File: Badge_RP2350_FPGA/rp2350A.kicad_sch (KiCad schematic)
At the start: 33 parts, among them J2 Conn_01x03_Pin, SW1 SW_Push, SW2 SW_Push, U1 RP2350_60QFN, U7 W25Q32JVSS, Y1 ABM8-272-T3

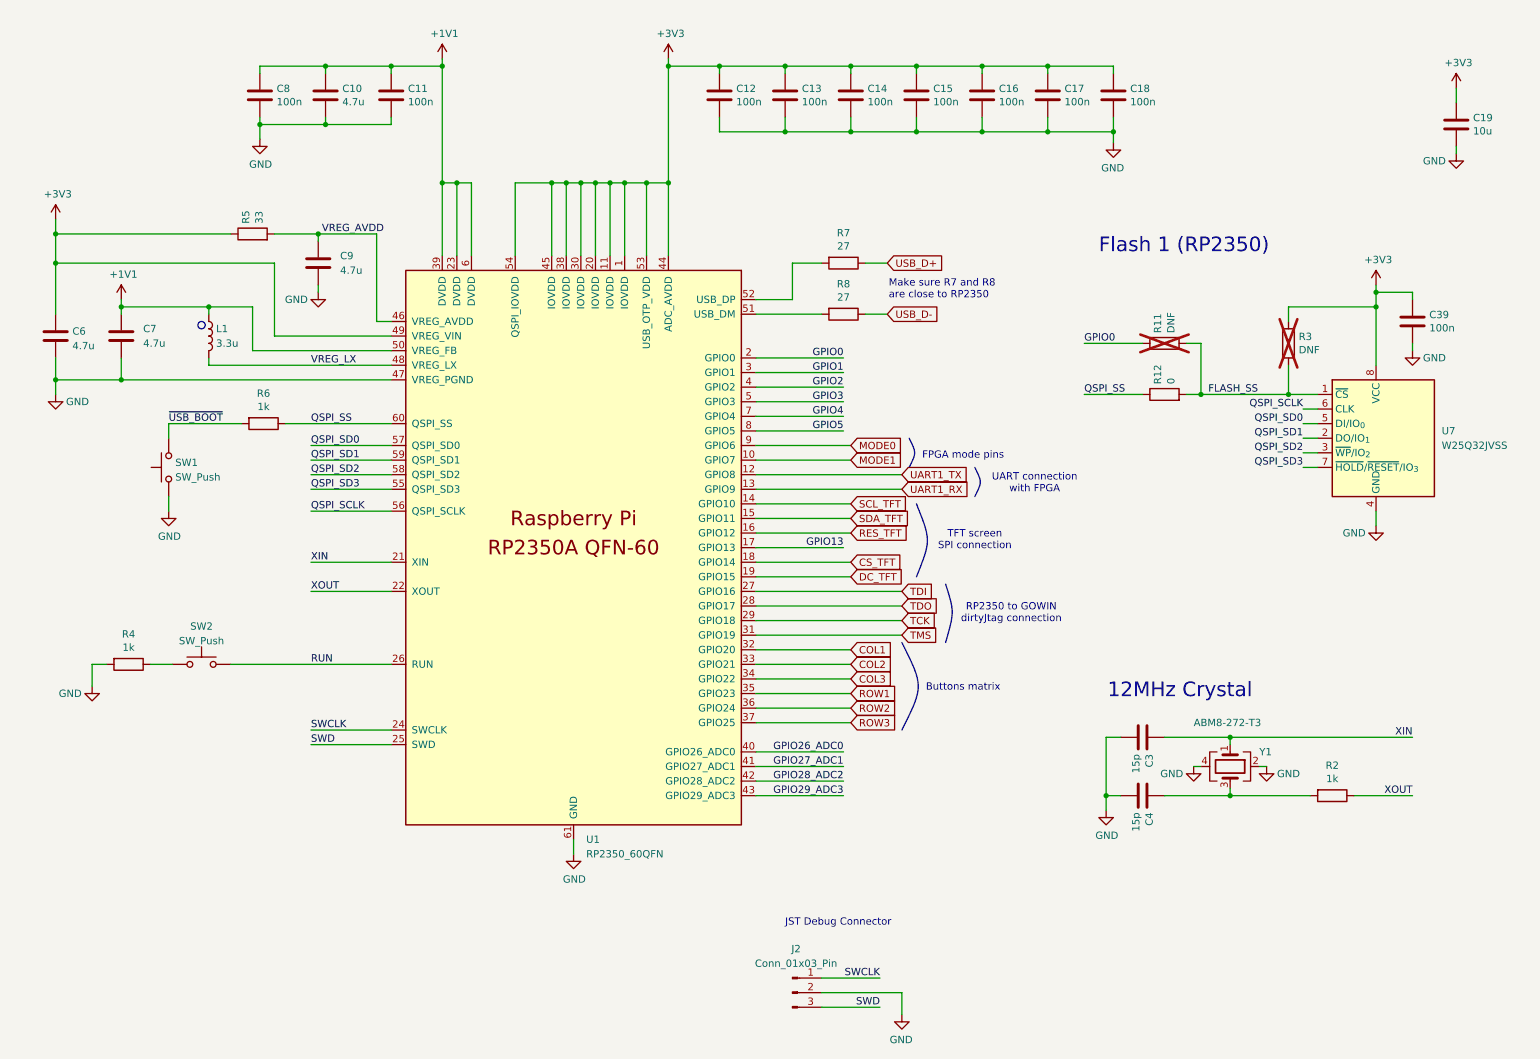
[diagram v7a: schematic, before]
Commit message: add headers and fix voltage references
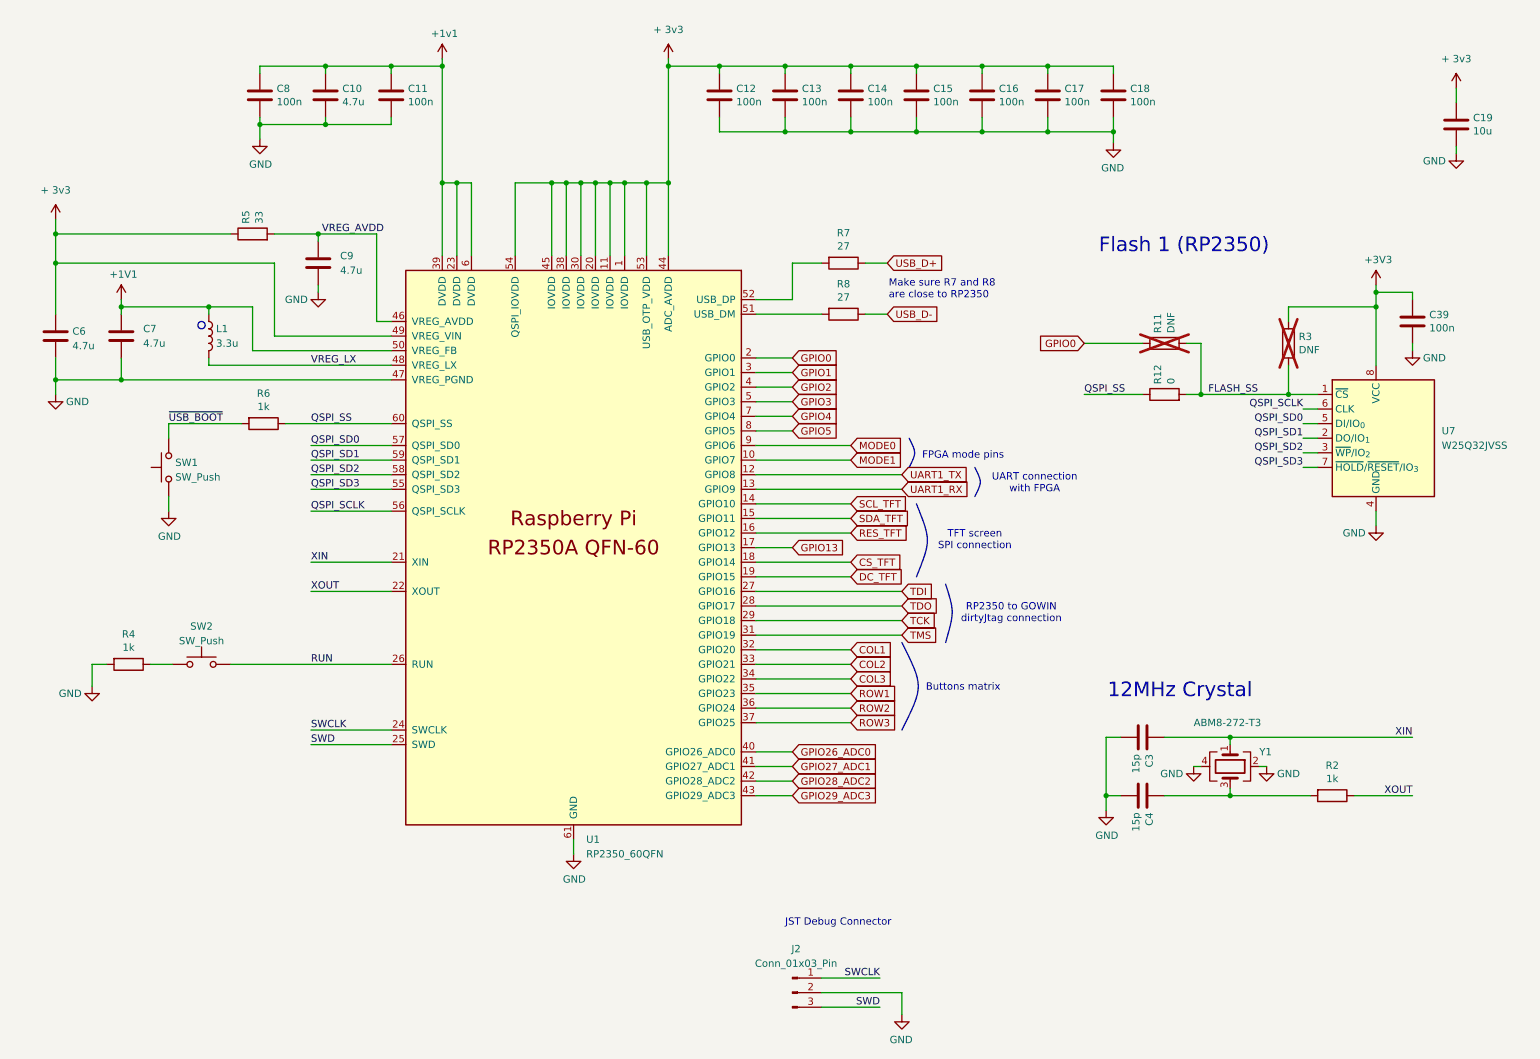
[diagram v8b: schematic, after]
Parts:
- J2: footprint Connector_PinHeader_1.00mm:PinHeader_1x03_P1.00mm_Vertical -> Connector_PinHeader_2.54mm:PinHeader_1x03_P2.54mm_Vertical
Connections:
- net +1V1: no longer C10.1, C11.1, C8.1, U1.23 (DVDD), U1.39 (DVDD), U1.6 (DVDD)
- net +3V3: no longer C12.1, C13.1, C14.1, C15.1, C16.1, C17.1, C18.1, C19.1, C6.1, R5.1, U1.1 (IOVDD), U1.11 (IOVDD), U1.20 (IOVDD), U1.30 (IOVDD), U1.38 (IOVDD), U1.44 (ADC_AVDD), U1.45 (IOVDD), U1.49 (VREG_VIN), U1.53 (USB_OTP_VDD), U1.54 (QSPI_IOVDD)
- new net + 3v3: C12.1, C13.1, C14.1, C15.1, C16.1, C17.1, C18.1, C19.1, C6.1, R5.1, U1.1 (IOVDD), U1.11 (IOVDD), U1.20 (IOVDD), U1.30 (IOVDD), U1.38 (IOVDD), U1.44 (ADC_AVDD), U1.45 (IOVDD), U1.49 (VREG_VIN), U1.53 (USB_OTP_VDD), U1.54 (QSPI_IOVDD)
- new net +1v1: C10.1, C11.1, C8.1, U1.23 (DVDD), U1.39 (DVDD), U1.6 (DVDD)
